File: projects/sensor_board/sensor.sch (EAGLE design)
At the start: 63 parts, among them J1 504050-0791, J2 FH28-10S-0.5SH_05_, J3 504050-0791, J4 504050-1091, J5 504050-0791, J6 504050-0791, U1 NXP_FXAS21002CQR1NXP_FXAS2100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, U2 HONEYWELL_HMC5983-TRHONEYWELL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, U3 DS1307N, U4 NXP_FXAS21002CQR1NXP_FXAS2100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, U5 HONEYWELL_HMC5983-TRHONEYWELL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, U6 NXP_FXAS21002CQR1NXP_FXAS2100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, U7 HONEYWELL_HMC5983-TRHONEYWELL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, Y1 ECS-.327-12.5-13X

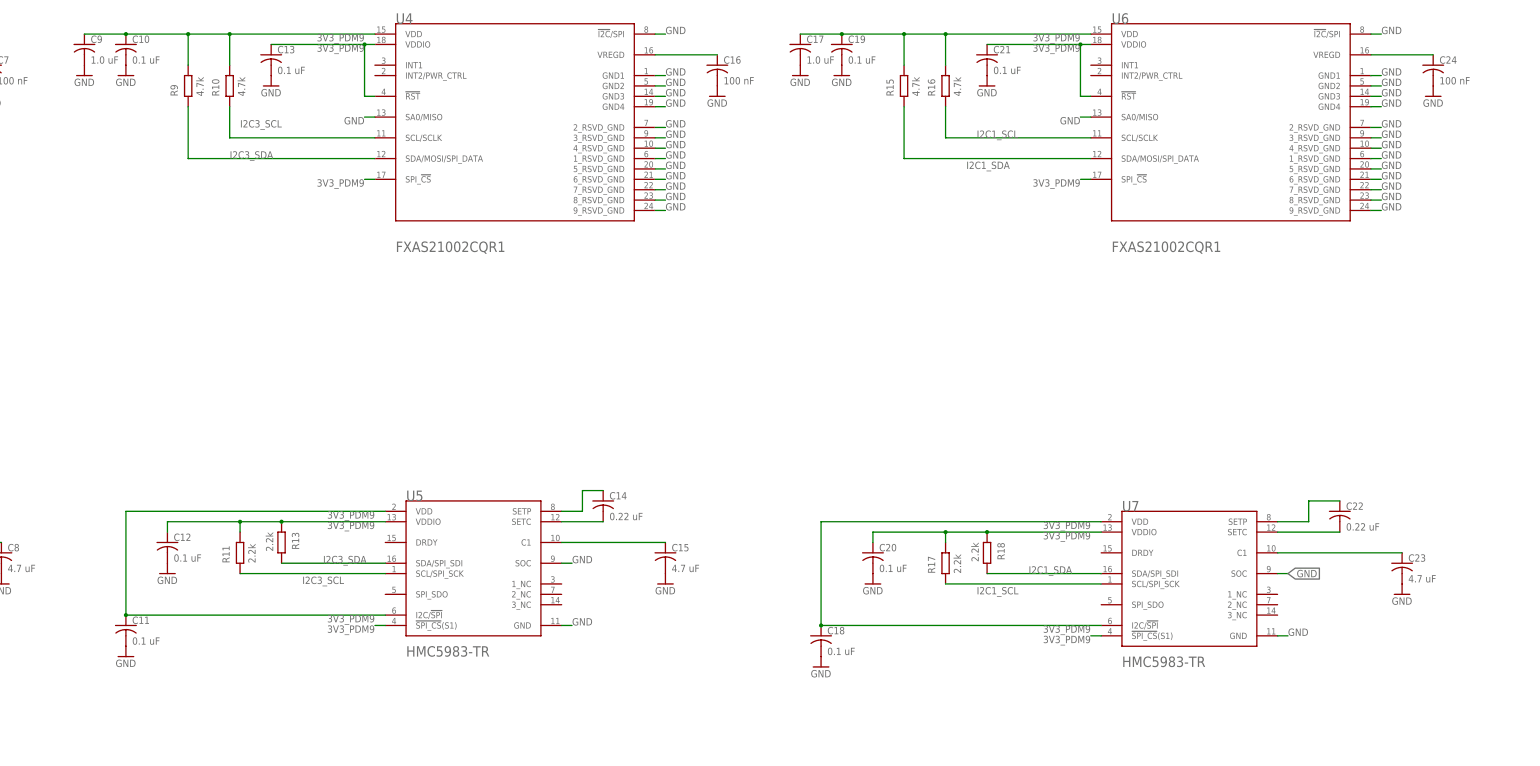
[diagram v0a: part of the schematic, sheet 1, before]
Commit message: Updates to sensor board. Routed sensors
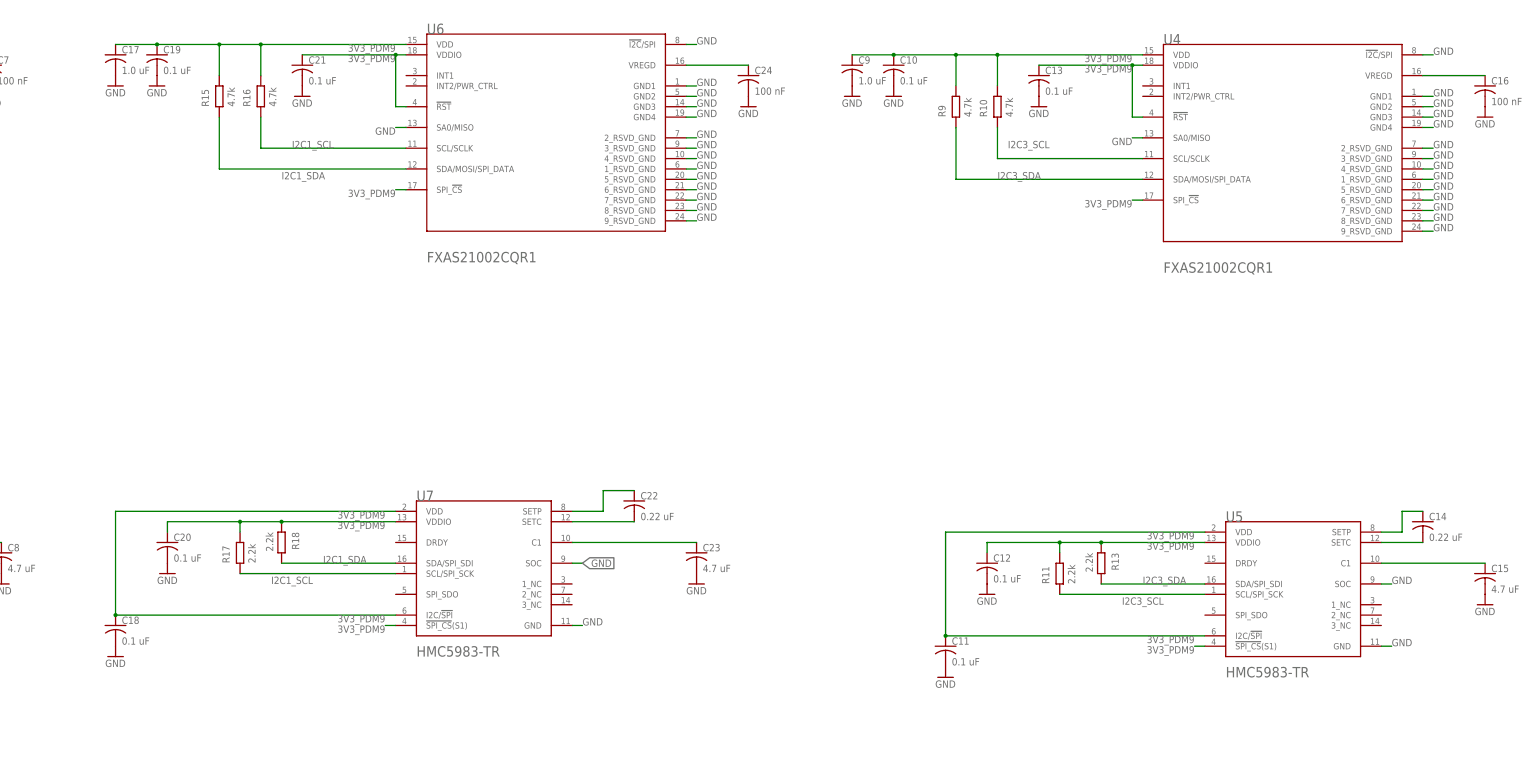
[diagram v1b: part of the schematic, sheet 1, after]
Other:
- moved on the sheet: C10, C11, C12, C13, C14, C15, C16, C17, C18, C19, C20, C21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

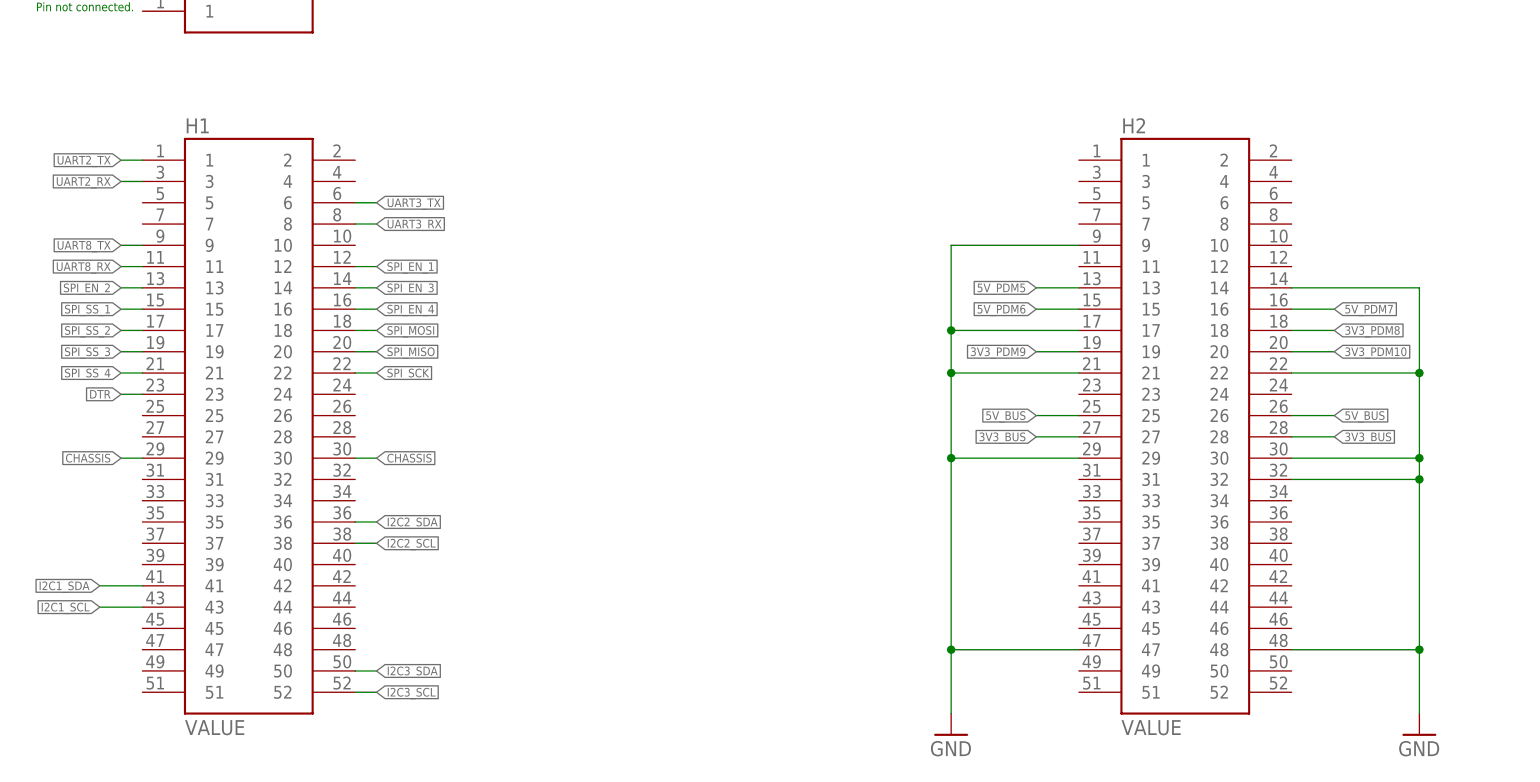
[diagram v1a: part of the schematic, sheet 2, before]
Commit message: Updated sensor board. First revision of completely routed board
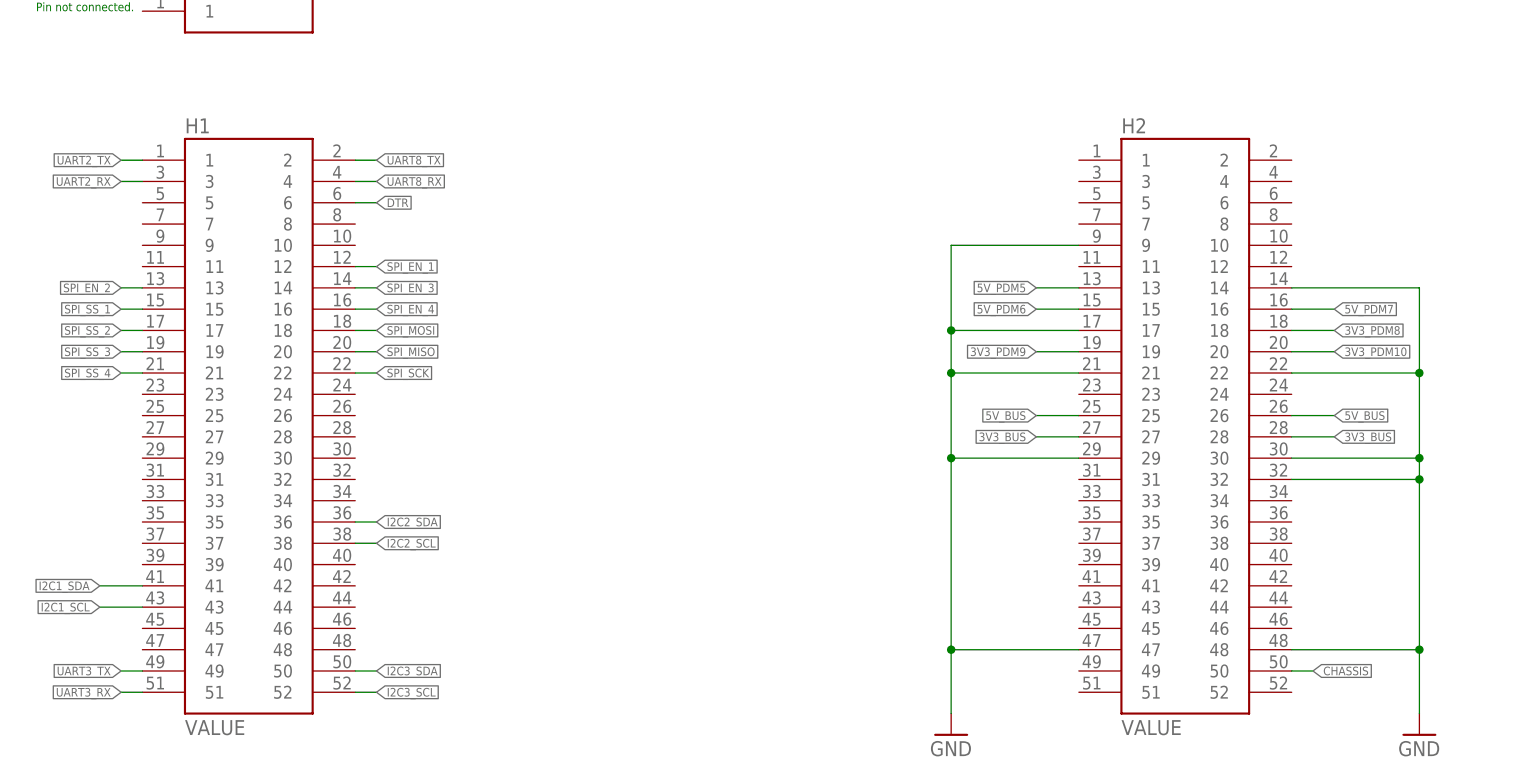
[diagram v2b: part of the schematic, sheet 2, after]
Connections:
- net CHASSIS: now also H2.50; no longer H1.29, H1.30
- net DTR: now also H1.6; no longer H1.23
- net UART3_RX: now also H1.51; no longer H1.8
- net UART3_TX: now also H1.49; no longer H1.6
- net UART8_RX: now also H1.4; no longer H1.11
- net UART8_TX: now also H1.2; no longer H1.9
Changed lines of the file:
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@@
 </segment>
 <segment>
-<pinref part="H1" gate="G$1" pin="23"/>
-<wire x1="40.64" y1="106.68" x2="38.1" y2="106.68" width="0.1524" layer="91"/>
-<label x="38.1" y="106.68" size="1.016" layer="95" rot="R180" xref="yes"/>
+<pinref part="H1" gate="G$1" pin="6"/>
+<wire x1="66.04" y1="129.54" x2="68.58" y2="129.54" width="0.1524" layer="91"/>
+<label x="68.58" y="129.54" size="1.016" layer="95" xref="yes"/>
 </segment>
 </net>
@@
 </segment>
 <segment>
-<pinref part="H1" gate="G$1" pin="9"/>
-<wire x1="40.64" y1="124.46" x2="38.1" y2="124.46" width="0.1524" layer="91"/>
-<label x="38.1" y="124.46" size="1.016" layer="95" rot="R180" xref="yes"/>
+<pinref part="H1" gate="G$1" pin="2"/>
+<wire x1="66.04" y1="134.62" x2="68.58" y2="134.62" width="0.1524" layer="91"/>
+<label x="68.58" y="134.62" size="1.016" layer="95" xref="yes"/>
 </segment>
 </net>
@@
 </segment>
 <segment>
-<pinref part="H1" gate="G$1" pin="11"/>
-<wire x1="40.64" y1="121.92" x2="38.1" y2="121.92" width="0.1524" layer="91"/>
-<label x="38.1" y="121.92" size="1.016" layer="95" rot="R180" xref="yes"/>
+<pinref part="H1" gate="G$1" pin="4"/>
+<wire x1="66.04" y1="132.08" x2="68.58" y2="132.08" width="0.1524" layer="91"/>
+<label x="68.58" y="132.08" size="1.016" layer="95" xref="yes"/>
 </segment>
 </net>
@@
 </segment>
 <segment>
-<pinref part="H1" gate="G$1" pin="6"/>
-<wire x1="66.04" y1="129.54" x2="68.58" y2="129.54" width="0.1524" layer="91"/>
-<label x="68.58" y="129.54" size="1.016" layer="95" xref="yes"/>
+<pinref part="H1" gate="G$1" pin="49"/>
+<wire x1="40.64" y1="73.66" x2="38.1" y2="73.66" width="0.1524" layer="91"/>
+<label x="38.1" y="73.66" size="1.016" layer="95" rot="R180" xref="yes"/>
 </segment>
 </net>
@@
 </segment>
 <segment>
-<pinref part="H1" gate="G$1" pin="8"/>
-<wire x1="66.04" y1="127" x2="68.58" y2="127" width="0.1524" layer="91"/>
-<label x="68.58" y="127" size="1.016" layer="95" xref="yes"/>
+<pinref part="H1" gate="G$1" pin="51"/>
+<wire x1="40.64" y1="71.12" x2="38.1" y2="71.12" width="0.1524" layer="91"/>
+<label x="38.1" y="71.12" size="1.016" layer="95" rot="R180" xref="yes"/>
 </segment>
 </net>
@@
 </segment>
 <segment>
-<pinref part="H1" gate="G$1" pin="30"/>
-<wire x1="66.04" y1="99.06" x2="68.58" y2="99.06" width="0.1524" layer="91"/>
-<label x="68.58" y="99.06" size="1.016" layer="95" xref="yes"/>
-</segment>
-<segment>
-<pinref part="H1" gate="G$1" pin="29"/>
-<wire x1="40.64" y1="99.06" x2="38.1" y2="99.06" width="0.1524" layer="91"/>
-<label x="38.1" y="99.06" size="1.016" layer="95" rot="R180" xref="yes"/>
+<pinref part="H2" gate="G$1" pin="50"/>
+<wire x1="177.8" y1="73.66" x2="180.34" y2="73.66" width="0.1524" layer="91"/>
+<label x="180.34" y="73.66" size="1.016" layer="95" xref="yes"/>
 </segment>
 </net>
@@
 </sheet>
 </sheets>
-<errors>
-</errors>
 </schematic>
 </drawing>

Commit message: Added oshpark 2 layer design rule, updated gyroscope library, added new gyroscope footprint to sensor board
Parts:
- U1, U4, U6: value NXP_FXAS21002CQR1NXP_FXAS21002CQR1_0_0 -> NXP_FXAS21002CQR1_EDITEDNXP_FXAS21002CQR1_0_0; device NXP - FXAS21002CQR1:NXP_FXAS21002CQR1NXP_FXAS21002CQR1_0_0 -> NXP - FXAS21002CQR1:NXP_FXAS21002CQR1_EDITEDNXP_FXAS21002CQR1_0_0
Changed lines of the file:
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@@
 <parts>
 <part name="FRAME1" library="frames" library_urn="urn:adsk.eagle:library:229" deviceset="FRAME_D_L" device="" value="PC104"/>
-<part name="U1" library="NXP - FXAS21002CQR1" deviceset="NXP_FXAS21002CQR1" device="NXP_FXAS21002CQR1_0_0"/>
+<part name="U1" library="NXP - FXAS21002CQR1" deviceset="NXP_FXAS21002CQR1_EDITED" device="NXP_FXAS21002CQR1_0_0"/>
 <part name="U2" library="Honeywell - HMC5983-TR" deviceset="HONEYWELL_HMC5983-TR" device="HONEYWELL_HMC5983-TR_0_0"/>
 <part name="U5" library="Honeywell - HMC5983-TR" deviceset="HONEYWELL_HMC5983-TR" device="HONEYWELL_HMC5983-TR_0_0"/>
@@
 <part name="R1" library="ngspice-simulation" library_urn="urn:adsk.eagle:library:527439" deviceset="R" device="" value="4.7k"/>
 <part name="R2" library="ngspice-simulation" library_urn="urn:adsk.eagle:library:527439" deviceset="R" device="" value="4.7k"/>
-<part name="U4" library="NXP - FXAS21002CQR1" deviceset="NXP_FXAS21002CQR1" device="NXP_FXAS21002CQR1_0_0"/>
+<part name="U4" library="NXP - FXAS21002CQR1" deviceset="NXP_FXAS21002CQR1_EDITED" device="NXP_FXAS21002CQR1_0_0"/>
 <part name="C10" library="rcl" library_urn="urn:adsk.eagle:library:334" deviceset="C-US" device="C0805" package3d_urn="urn:adsk.eagle:package:23617/2" value="0.1 uF"/>
 <part name="GND13" library="supply1" library_urn="urn:adsk.eagle:library:371" deviceset="GND" device=""/>
@@
 <part name="R9" library="ngspice-simulation" library_urn="urn:adsk.eagle:library:527439" deviceset="R" device="" value="4.7k"/>
 <part name="R10" library="ngspice-simulation" library_urn="urn:adsk.eagle:library:527439" deviceset="R" device="" value="4.7k"/>
-<part name="U6" library="NXP - FXAS21002CQR1" deviceset="NXP_FXAS21002CQR1" device="NXP_FXAS21002CQR1_0_0"/>
+<part name="U6" library="NXP - FXAS21002CQR1" deviceset="NXP_FXAS21002CQR1_EDITED" device="NXP_FXAS21002CQR1_0_0"/>
 <part name="C19" library="rcl" library_urn="urn:adsk.eagle:library:334" deviceset="C-US" device="C0805" package3d_urn="urn:adsk.eagle:package:23617/2" value="0.1 uF"/>
 <part name="GND22" library="supply1" library_urn="urn:adsk.eagle:library:371" deviceset="GND" device=""/>

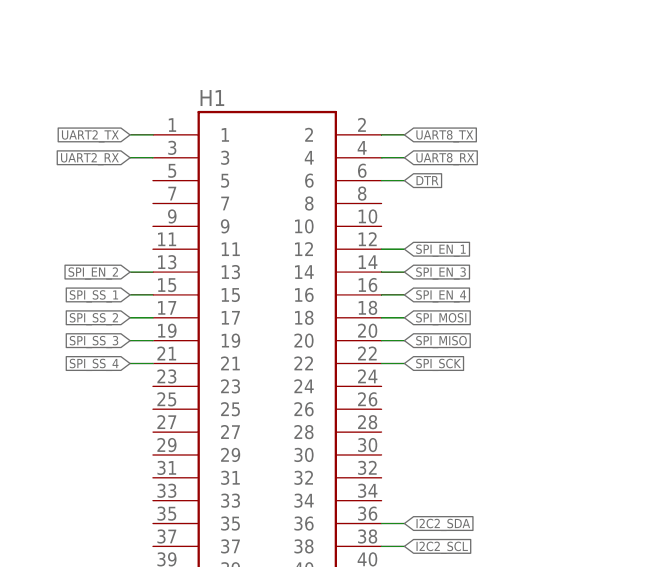
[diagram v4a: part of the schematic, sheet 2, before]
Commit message: Completed first revision of 4 layer sensor board
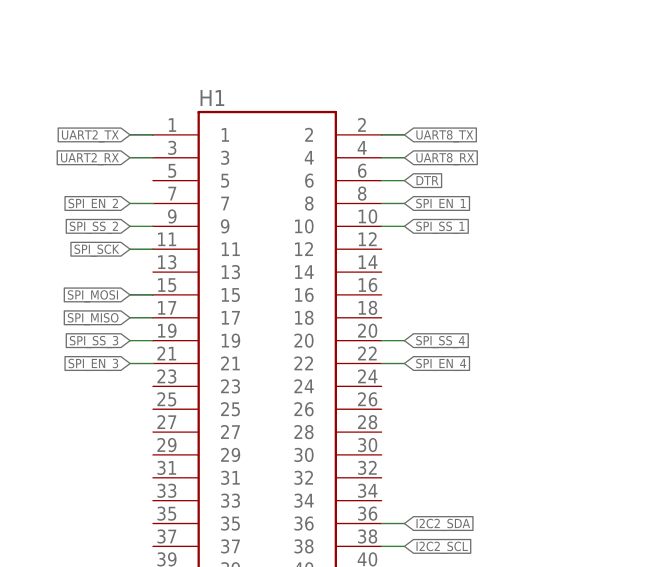
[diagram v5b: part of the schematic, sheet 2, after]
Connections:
- net SPI_EN_1: now also H1.8; no longer H1.12
- net SPI_EN_2: now also H1.7; no longer H1.13
- net SPI_EN_3: now also H1.21; no longer H1.14
- net SPI_EN_4: now also H1.22; no longer H1.16
- net SPI_MISO: now also H1.17; no longer H1.20
- net SPI_MOSI: now also H1.15; no longer H1.18
- net SPI_SCK: now also H1.11; no longer H1.22
- net SPI_SS_1: now also H1.10; no longer H1.15
- net SPI_SS_2: now also H1.9; no longer H1.17
- net SPI_SS_4: now also H1.20; no longer H1.21
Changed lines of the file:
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@@
 </segment>
 <segment>
-<pinref part="H1" gate="G$1" pin="13"/>
-<wire x1="40.64" y1="119.38" x2="38.1" y2="119.38" width="0.1524" layer="91"/>
-<label x="38.1" y="119.38" size="1.016" layer="95" rot="R180" xref="yes"/>
+<pinref part="H1" gate="G$1" pin="7"/>
+<wire x1="40.64" y1="127" x2="38.1" y2="127" width="0.1524" layer="91"/>
+<label x="38.1" y="127" size="1.016" layer="95" rot="R180" xref="yes"/>
 </segment>
 </net>
@@
 </segment>
 <segment>
-<pinref part="H1" gate="G$1" pin="15"/>
-<wire x1="40.64" y1="116.84" x2="38.1" y2="116.84" width="0.1524" layer="91"/>
-<label x="38.1" y="116.84" size="1.016" layer="95" rot="R180" xref="yes"/>
+<pinref part="H1" gate="G$1" pin="10"/>
+<wire x1="66.04" y1="124.46" x2="68.58" y2="124.46" width="0.1524" layer="91"/>
+<label x="68.58" y="124.46" size="1.016" layer="95" xref="yes"/>
 </segment>
 </net>
@@
 </segment>
 <segment>
-<pinref part="H1" gate="G$1" pin="17"/>
-<wire x1="40.64" y1="114.3" x2="38.1" y2="114.3" width="0.1524" layer="91"/>
-<label x="38.1" y="114.3" size="1.016" layer="95" rot="R180" xref="yes"/>
+<pinref part="H1" gate="G$1" pin="9"/>
+<wire x1="40.64" y1="124.46" x2="38.1" y2="124.46" width="0.1524" layer="91"/>
+<label x="38.1" y="124.46" size="1.016" layer="95" rot="R180" xref="yes"/>
 </segment>
 </net>
@@
 </segment>
 <segment>
-<pinref part="H1" gate="G$1" pin="21"/>
-<wire x1="40.64" y1="109.22" x2="38.1" y2="109.22" width="0.1524" layer="91"/>
-<label x="38.1" y="109.22" size="1.016" layer="95" rot="R180" xref="yes"/>
+<pinref part="H1" gate="G$1" pin="20"/>
+<wire x1="66.04" y1="111.76" x2="68.58" y2="111.76" width="0.1524" layer="91"/>
+<label x="68.58" y="111.76" size="1.016" layer="95" xref="yes"/>
 </segment>
 </net>
@@
 </segment>
 <segment>
-<pinref part="H1" gate="G$1" pin="12"/>
-<wire x1="66.04" y1="121.92" x2="68.58" y2="121.92" width="0.1524" layer="91"/>
-<label x="68.58" y="121.92" size="1.016" layer="95" xref="yes"/>
+<pinref part="H1" gate="G$1" pin="8"/>
+<wire x1="66.04" y1="127" x2="68.58" y2="127" width="0.1524" layer="91"/>
+<label x="68.58" y="127" size="1.016" layer="95" xref="yes"/>
 </segment>
 </net>
@@
 </segment>
 <segment>
-<pinref part="H1" gate="G$1" pin="14"/>
-<wire x1="66.04" y1="119.38" x2="68.58" y2="119.38" width="0.1524" layer="91"/>
-<label x="68.58" y="119.38" size="1.016" layer="95" xref="yes"/>
+<pinref part="H1" gate="G$1" pin="21"/>
+<wire x1="40.64" y1="109.22" x2="38.1" y2="109.22" width="0.1524" layer="91"/>
+<label x="38.1" y="109.22" size="1.016" layer="95" rot="R180" xref="yes"/>
 </segment>
 </net>
@@
 </segment>
 <segment>
-<pinref part="H1" gate="G$1" pin="16"/>
-<wire x1="66.04" y1="116.84" x2="68.58" y2="116.84" width="0.1524" layer="91"/>
-<label x="68.58" y="116.84" size="1.016" layer="95" xref="yes"/>
+<pinref part="H1" gate="G$1" pin="22"/>
+<wire x1="66.04" y1="109.22" x2="68.58" y2="109.22" width="0.1524" layer="91"/>
+<label x="68.58" y="109.22" size="1.016" layer="95" xref="yes"/>
 </segment>
 </net>
@@
 </segment>
 <segment>
-<pinref part="H1" gate="G$1" pin="18"/>
-<wire x1="66.04" y1="114.3" x2="68.58" y2="114.3" width="0.1524" layer="91"/>
-<label x="68.58" y="114.3" size="1.016" layer="95" xref="yes"/>
+<pinref part="H1" gate="G$1" pin="15"/>
+<wire x1="40.64" y1="116.84" x2="38.1" y2="116.84" width="0.1524" layer="91"/>
+<label x="38.1" y="116.84" size="1.016" layer="95" rot="R180" xref="yes"/>
 </segment>
 </net>
@@
 </segment>
 <segment>
-<pinref part="H1" gate="G$1" pin="20"/>
-<wire x1="66.04" y1="111.76" x2="68.58" y2="111.76" width="0.1524" layer="91"/>
-<label x="68.58" y="111.76" size="1.016" layer="95" xref="yes"/>
+<pinref part="H1" gate="G$1" pin="17"/>
+<wire x1="40.64" y1="114.3" x2="38.1" y2="114.3" width="0.1524" layer="91"/>
+<label x="38.1" y="114.3" size="1.016" layer="95" rot="R180" xref="yes"/>
 </segment>
 </net>
@@
 </segment>
 <segment>
-<pinref part="H1" gate="G$1" pin="22"/>
-<wire x1="66.04" y1="109.22" x2="68.58" y2="109.22" width="0.1524" layer="91"/>
-<label x="68.58" y="109.22" size="1.016" layer="95" xref="yes"/>
+<pinref part="H1" gate="G$1" pin="11"/>
+<wire x1="40.64" y1="121.92" x2="38.1" y2="121.92" width="0.1524" layer="91"/>
+<label x="38.1" y="121.92" size="1.016" layer="95" rot="R180" xref="yes"/>
 </segment>
 </net>
